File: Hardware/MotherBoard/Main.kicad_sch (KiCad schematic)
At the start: 12 parts, among them J11 DMA_PULLUP, U2 AT28C256, U3 WD65C22, U4 AS6C62256, U5 WD65C02

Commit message: Fix
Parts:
- added R7: 3K3, Resistor_THT:R_Axial_DIN0207_L6.3mm_D2.5mm_P10.16mm_Horizontal, symbol Device:R
- R2, R5: value 10K -> 3K3
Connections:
- net +5V: now also R7.1; no longer J11.2 (Pin_2)
- new net: J11.2 (Pin_2), R7.2
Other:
- title: Retro 6502 Mother Board -> Miniish
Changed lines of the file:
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@@
   (paper "A4")
   (title_block
-    (title "Retro 6502 Mother Board")
-    (rev "0.1")
+    (title "Miniish")
+    (rev "v1.2b")
     (company "Romuald Rousseau")
   )
@@
   (junction (at 135.382 94.996) (diameter 1.016) (color 0 0 0 0))
   (no_connect (at 51.816 120.65))
+  (no_connect (at 84.836 123.19))
+  (no_connect (at 51.816 135.89))
+  (no_connect (at 51.816 130.81))
   (no_connect (at 51.816 125.73))
-  (no_connect (at 51.816 135.89))
-  (no_connect (at 84.836 123.19))
-  (no_connect (at 51.816 130.81))
   (bus_entry (at 29.21 33.02) (size 2.54 -2.54)
     (stroke (width 0.1524) (type solid) (color 0 0 0 0))
@@
     (stroke (width 0) (type solid) (color 0 0 0 0))
   )
-  (wire (pts (xy 131.064 147.066) (xy 131.064 159.258))
+  (wire (pts (xy 131.064 147.066) (xy 131.064 148.59))
+    (stroke (width 0) (type solid) (color 0 0 0 0))
+  )
+  (wire (pts (xy 131.064 156.21) (xy 131.064 159.258))
     (stroke (width 0) (type solid) (color 0 0 0 0))
   )
@@
     (in_bom yes) (on_board yes)
     (property "Reference" "R5" (id 0) (at 45.466 118.11 90))
-    (property "Value" "10K" (id 1) (at 45.466 120.65 90))
+    (property "Value" "3K3" (id 1) (at 45.466 120.65 90))
     (property "Footprint" "Resistor_THT:R_Axial_DIN0207_L6.3mm_D2.5mm_P10.16mm_Horizontal" (id 2) (at 45.466 121.412 90)
       (effects (font (size 1.27 1.27)) hide)
@@
     (in_bom yes) (on_board yes)
     (property "Reference" "R2" (id 0) (at 97.282 120.65 90))
-    (property "Value" "10K" (id 1) (at 97.282 123.19 90))
+    (property "Value" "3K3" (id 1) (at 97.282 123.19 90))
     (property "Footprint" "Resistor_THT:R_Axial_DIN0207_L6.3mm_D2.5mm_P10.16mm_Horizontal" (id 2) (at 97.536 123.952 90)
       (effects (font (size 1.27 1.27)) hide)
@@
       (effects (font (size 1.27 1.27)) hide)
     )
+  )
+  (symbol (lib_id "Device:R") (at 131.064 152.4 0) (unit 1)
+    (in_bom yes) (on_board yes)
+    (property "Reference" "R7" (id 0) (at 125.984 152.654 90))
+    (property "Value" "3K3" (id 1) (at 128.524 152.654 90))
+    (property "Footprint" "Resistor_THT:R_Axial_DIN0207_L6.3mm_D2.5mm_P10.16mm_Horizontal" (id 2) (at 129.286 152.4 90)
+      (effects (font (size 1.27 1.27)) hide)
+    )
+    (property "Datasheet" "" (id 3) (at 131.064 152.4 0)
+      (effects (font (size 1.27 1.27)) hide)
+    )

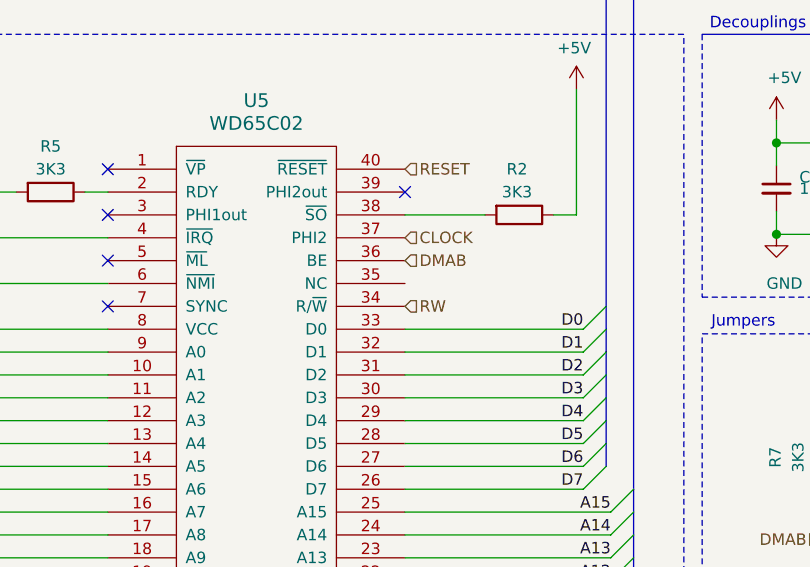
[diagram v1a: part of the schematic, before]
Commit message: Update to Kicad 6.0
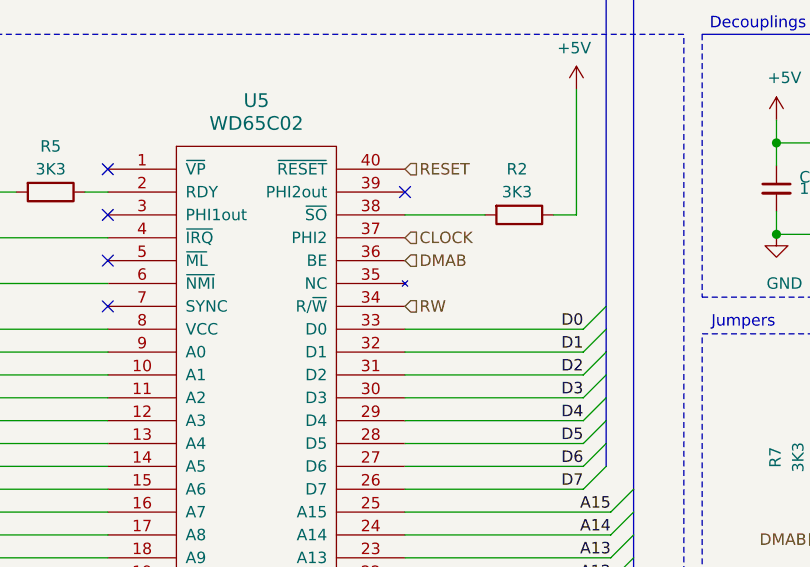
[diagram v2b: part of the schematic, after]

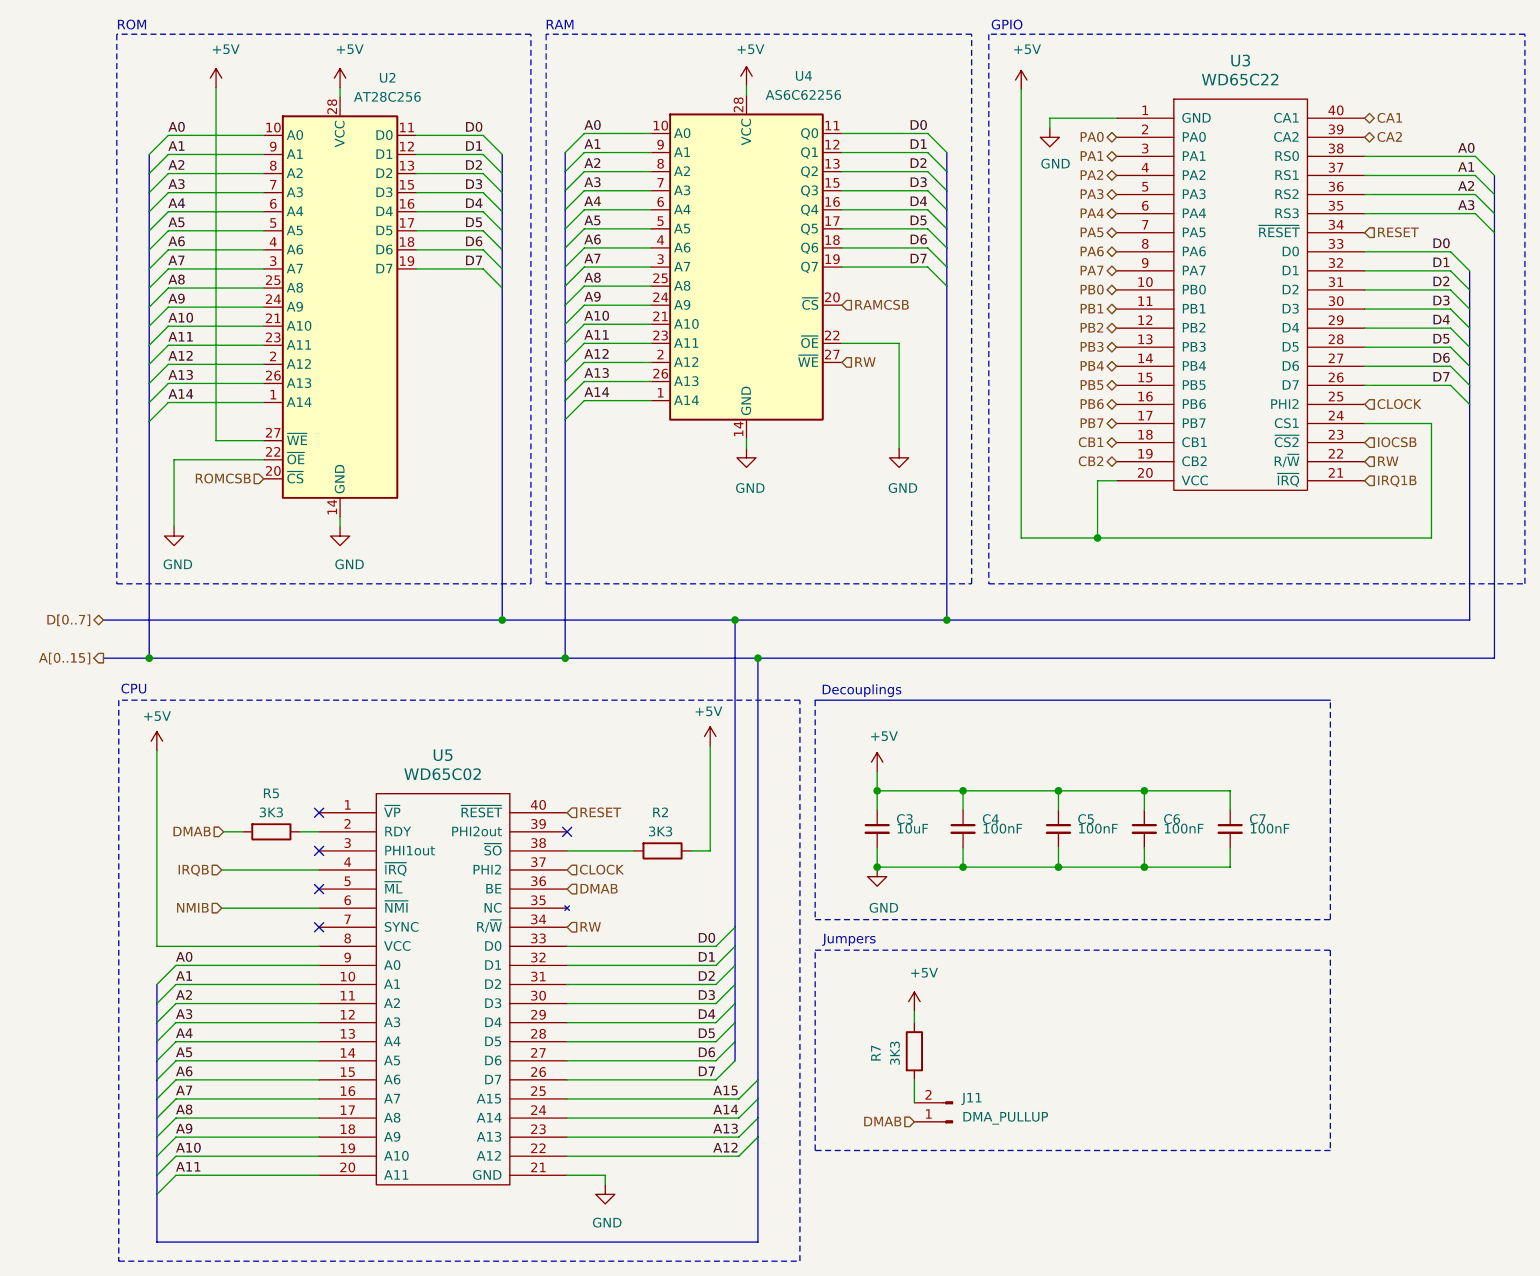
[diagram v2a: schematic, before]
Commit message: Fix Reset, WAI Signal, Add PROG jumper and reformat luc files
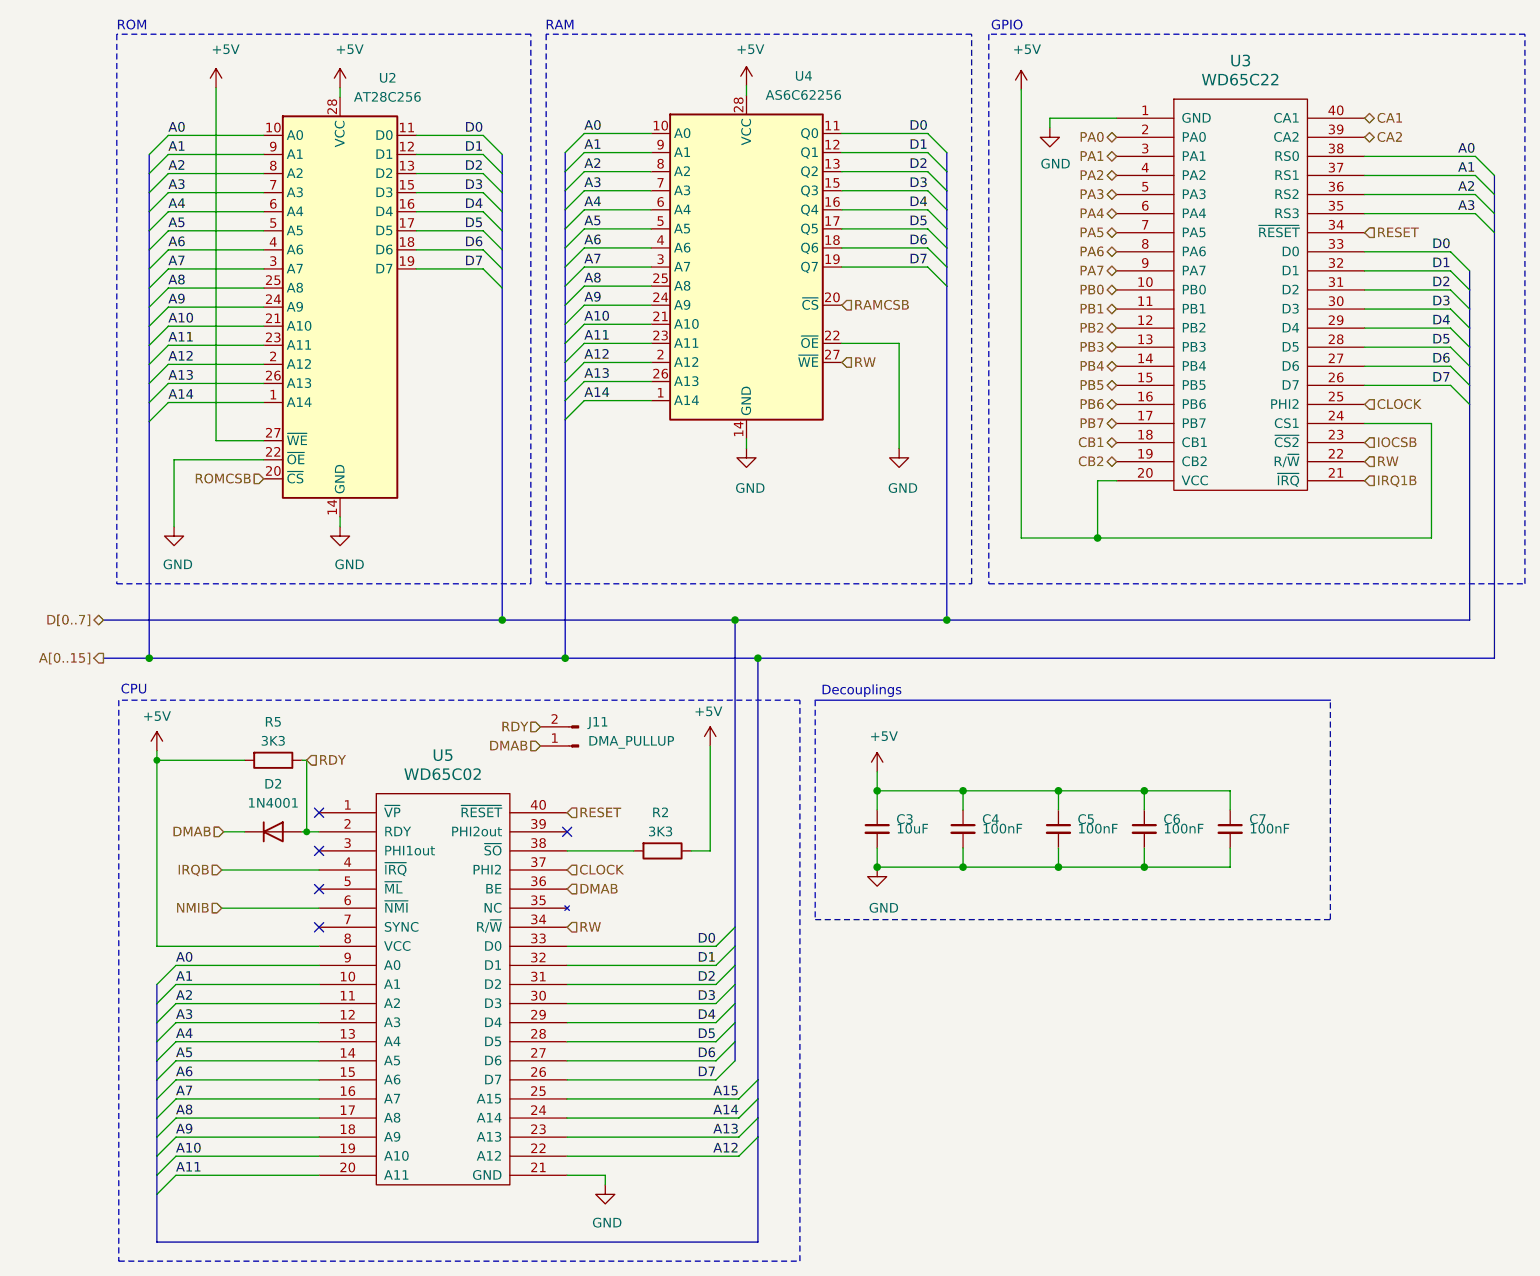
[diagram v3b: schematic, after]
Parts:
- removed R7: 3K3, Resistor_THT:R_Axial_DIN0207_L6.3mm_D2.5mm_P10.16mm_Horizontal, symbol Device:R
- added D2: 1N4001, Diode_THT:D_DO-41_SOD81_P10.16mm_Horizontal, symbol Diode:1N4001
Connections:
- net +5V: now also R5.2
- net DMAB: now also D2.1 (K); no longer R5.2
- net RDY: now reaches J11.2 (Pin_2)
- net RDY: now also R5.1, U5.2 (RDY), D2.2 (A)
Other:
- note removed: "Jumpers"
- moved on the sheet: J11, R5
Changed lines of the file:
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@@
     (company "Romuald Rousseau")
   )
+  (bus_alias "A" (members "A0" "A1" "A2" "A3" "A4" "A5" "A6" "A7"))
   (bus_alias "D" (members "D0" "D1" "D2"))
-  (bus_alias "A" (members "A0" "A1" "A2" "A3" "A4" "A5" "A6" "A7"))
   (junction (at 150.241 117.729) (diameter 1.016) (color 0 0 0 0)
   )
@@
   (junction (at 110.236 100.076) (diameter 1.016) (color 0 0 0 0)
   )
+  (junction (at 30.226 113.665) (diameter 0) (color 0 0 0 0)
+  )
   (junction (at 150.241 127.889) (diameter 1.016) (color 0 0 0 0)
   )
@@
   )
   (junction (at 84.582 100.076) (diameter 1.016) (color 0 0 0 0)
+  )
+  (junction (at 50.165 123.19) (diameter 0) (color 0 0 0 0)
   )
   (junction (at 137.541 127.889) (diameter 1.016) (color 0 0 0 0)
@@
     (stroke (width 0.1524) (type solid) (color 0 0 0 0))
   )
-  (polyline (pts (xy 186.436 138.938) (xy 186.436 165.608))
-    (stroke (width 0) (type dash) (color 0 0 0 0))
-  )
   (wire (pts (xy 173.101 127.889) (xy 173.101 125.349))
     (stroke (width 0) (type solid) (color 0 0 0 0))
@@
   (wire (pts (xy 31.75 55.88) (xy 44.45 55.88))
     (stroke (width 0) (type solid) (color 0 0 0 0))
-  )
-  (polyline (pts (xy 117.856 165.608) (xy 117.856 138.938))
-    (stroke (width 0) (type dash) (color 0 0 0 0))
   )
   (wire (pts (xy 31.75 53.34) (xy 44.45 53.34))
@@
     (stroke (width 0) (type solid) (color 0 0 0 0))
   )
+  (wire (pts (xy 30.226 113.665) (xy 30.226 138.43))
+    (stroke (width 0) (type solid) (color 0 0 0 0))
+  )
   (wire (pts (xy 121.412 35.306) (xy 132.842 35.306))
     (stroke (width 0) (type solid) (color 0 0 0 0))
   )
   (wire (pts (xy 191.008 40.894) (xy 205.74 40.894))
-    (stroke (width 0) (type solid) (color 0 0 0 0))
-  )
-  (wire (pts (xy 131.064 147.066) (xy 131.064 148.59))
     (stroke (width 0) (type solid) (color 0 0 0 0))
   )
@@
     (stroke (width 0) (type solid) (color 0 0 0 0))
   )
+  (wire (pts (xy 50.165 113.665) (xy 50.165 123.19))
+    (stroke (width 0) (type default) (color 0 0 0 0))
+  )
   (wire (pts (xy 191.008 56.134) (xy 202.438 56.134))
     (stroke (width 0) (type solid) (color 0 0 0 0))
@@
   (bus (pts (xy 208.28 35.814) (xy 208.28 38.354))
     (stroke (width 0) (type solid) (color 0 0 0 0))
+  )
+  (wire (pts (xy 50.165 123.19) (xy 51.816 123.19))
+    (stroke (width 0) (type default) (color 0 0 0 0))
   )
   (bus (pts (xy 29.21 100.076) (xy 84.582 100.076))
@@
     (stroke (width 0) (type solid) (color 0 0 0 0))
   )
-  (polyline (pts (xy 186.436 165.608) (xy 117.856 165.608))
-    (stroke (width 0) (type dash) (color 0 0 0 0))
-  )
   (wire (pts (xy 54.61 81.28) (xy 54.61 82.55))
     (stroke (width 0) (type solid) (color 0 0 0 0))
@@
     (stroke (width 0) (type solid) (color 0 0 0 0))
   )
+  (wire (pts (xy 49.53 113.665) (xy 50.165 113.665))
+    (stroke (width 0) (type default) (color 0 0 0 0))
+  )
   (wire (pts (xy 84.836 140.97) (xy 104.648 140.97))
     (stroke (width 0) (type solid) (color 0 0 0 0))
@@
     (stroke (width 0) (type solid) (color 0 0 0 0))
   )
-  (wire (pts (xy 30.226 138.43) (xy 30.226 112.395))
+  (wire (pts (xy 30.226 112.395) (xy 30.226 113.665))
     (stroke (width 0) (type solid) (color 0 0 0 0))
   )
@@
     (stroke (width 0) (type solid) (color 0 0 0 0))
   )
-  (wire (pts (xy 49.276 123.19) (xy 51.816 123.19))
-    (stroke (width 0) (type solid) (color 0 0 0 0))
-  )
   (bus (pts (xy 30.226 158.75) (xy 30.226 161.29))
     (stroke (width 0) (type solid) (color 0 0 0 0))
@@
     (stroke (width 0) (type solid) (color 0 0 0 0))
   )
+  (wire (pts (xy 49.53 123.19) (xy 50.165 123.19))
+    (stroke (width 0) (type default) (color 0 0 0 0))
+  )
   (wire (pts (xy 87.122 48.006) (xy 96.012 48.006))
     (stroke (width 0) (type solid) (color 0 0 0 0))
@@
     (stroke (width 0) (type solid) (color 0 0 0 0))
   )
-  (wire (pts (xy 39.116 123.19) (xy 41.656 123.19))
+  (wire (pts (xy 39.116 123.19) (xy 41.91 123.19))
     (stroke (width 0) (type solid) (color 0 0 0 0))
   )
@@
     (stroke (width 0) (type solid) (color 0 0 0 0))
   )
-  (polyline (pts (xy 117.856 138.938) (xy 186.436 138.938))
-    (stroke (width 0) (type dash) (color 0 0 0 0))
-  )
   (bus (pts (xy 107.188 148.59) (xy 107.188 151.13))
     (stroke (width 0) (type solid) (color 0 0 0 0))
@@
     (stroke (width 0) (type solid) (color 0 0 0 0))
   )
+  (wire (pts (xy 41.91 113.665) (xy 30.226 113.665))
+    (stroke (width 0) (type default) (color 0 0 0 0))
+  )
   (wire (pts (xy 191.008 68.834) (xy 199.898 68.834))
     (stroke (width 0) (type solid) (color 0 0 0 0))
   )
   (wire (pts (xy 145.288 24.384) (xy 145.288 84.074))
-    (stroke (width 0) (type solid) (color 0 0 0 0))
-  )
-  (wire (pts (xy 131.064 156.21) (xy 131.064 159.258))
     (stroke (width 0) (type solid) (color 0 0 0 0))
   )
@@
     (effects (font (size 1.27 1.27)) (justify right bottom))
   )
-  (text "Jumpers" (at 125.984 138.43 180)
-    (effects (font (size 1.27 1.27)) (justify right bottom))
-  )
   (text "RAM" (at 85.852 16.764 180)
     (effects (font (size 1.27 1.27)) (justify right bottom))
@@
     (effects (font (size 1.27 1.27)) (justify right))
   )
-  (hierarchical_label "DMAB" (shape input) (at 131.064 161.798 180)
+  (hierarchical_label "DMAB" (shape input) (at 81.28 111.76 180)
     (effects (font (size 1.27 1.27)) (justify right))
   )
@@
     (effects (font (size 1.27 1.27)) (justify right))
   )
+  (hierarchical_label "RDY" (shape input) (at 50.165 113.665 0)
+    (effects (font (size 1.27 1.27)) (justify left))
+  )
   (hierarchical_label "RW" (shape input) (at 84.836 135.89 0)
     (effects (font (size 1.27 1.27)) (justify left))
   )
+  (hierarchical_label "RDY" (shape input) (at 81.28 109.22 180)
+    (effects (font (size 1.27 1.27)) (justify right))
+  )
   (hierarchical_label "RAMCSB" (shape input) (at 121.412 53.086 0)
     (effects (font (size 1.27 1.27)) (justify left))
@@
     )
     (property "Datasheet" "" (id 3) (at 108.712 23.876 0)
-      (effects (font (size 1.27 1.27)) hide)
-    )
-    (pin "1")
-  )
-  (symbol (lib_id "power:+5V") (at 131.064 147.066 0) (unit 1)
-    (in_bom yes) (on_board yes)
-    (property "Reference" "#PWR08" (id 0) (at 131.064 150.876 0)
-      (effects (font (size 1.27 1.27)) hide)
-    )
-    (property "Value" "+5V" (id 1) (at 132.334 141.986 0))
-    (property "Footprint" "" (id 2) (at 131.064 147.066 0)
-      (effects (font (size 1.27 1.27)) hide)
-    )
-    (property "Datasheet" "" (id 3) (at 131.064 147.066 0)
       (effects (font (size 1.27 1.27)) hide)
     )
@@
     (pin "1")
   )
-  (symbol (lib_id "Device:R") (at 131.064 152.4 0) (unit 1)
-    (in_bom yes) (on_board yes)
-    (property "Reference" "R7" (id 0) (at 125.984 152.654 90))
-    (property "Value" "3K3" (id 1) (at 128.524 152.654 90))
-    (property "Footprint" "Resistor_THT:R_Axial_DIN0207_L6.3mm_D2.5mm_P10.16mm_Horizontal" (id 2) (at 129.286 152.4 90)
-      (effects (font (size 1.27 1.27)) hide)
-    )
-    (property "Datasheet" "" (id 3) (at 131.064 152.4 0)
-      (effects (font (size 1.27 1.27)) hide)
-    )
-    (pin "1")
-    (pin "2")
-  )
-  (symbol (lib_id "Device:R") (at 45.466 123.19 270) (unit 1)
-    (in_bom yes) (on_board yes)
-    (property "Reference" "R5" (id 0) (at 45.466 118.11 90))
-    (property "Value" "3K3" (id 1) (at 45.466 120.65 90))
-    (property "Footprint" "Resistor_THT:R_Axial_DIN0207_L6.3mm_D2.5mm_P10.16mm_Horizontal" (id 2) (at 45.466 121.412 90)
-      (effects (font (size 1.27 1.27)) hide)
-    )
-    (property "Datasheet" "" (id 3) (at 45.466 123.19 0)
+  (symbol (lib_id "Device:R") (at 45.72 113.665 270) (unit 1)
+    (in_bom yes) (on_board yes)
+    (property "Reference" "R5" (id 0) (at 45.72 108.585 90))
+    (property "Value" "3K3" (id 1) (at 45.72 111.125 90))
+    (property "Footprint" "Resistor_THT:R_Axial_DIN0207_L6.3mm_D2.5mm_P10.16mm_Horizontal" (id 2) (at 45.72 111.887 90)
+      (effects (font (size 1.27 1.27)) hide)
+    )
+    (property "Datasheet" "" (id 3) (at 45.72 113.665 0)
       (effects (font (size 1.27 1.27)) hide)
     )
@@
     (pin "9")
   )
-  (symbol (lib_id "Connector:Conn_01x02_Male") (at 136.144 161.798 180) (unit 1)
-    (in_bom yes) (on_board yes)
-    (property "Reference" "J11" (id 0) (at 137.414 158.623 0)
+  (symbol (lib_id "Diode:1N4001") (at 45.72 123.19 0) (unit 1)
+    (in_bom yes) (on_board yes) (fields_autoplaced)
+    (property "Reference" "D2" (id 0) (at 45.72 116.84 0))
+    (property "Value" "1N4001" (id 1) (at 45.72 119.38 0))
+    (property "Footprint" "Diode_THT:D_DO-41_SOD81_P10.16mm_Horizontal" (id 2) (at 45.72 127.635 0)
+      (effects (font (size 1.27 1.27)) hide)
+    )
+    (property "Datasheet" "http://www.vishay.com/docs/88503/1n4001.pdf" (id 3) (at 45.72 123.19 0)
+      (effects (font (size 1.27 1.27)) hide)
+    )
+    (pin "1")
+    (pin "2")
+  )
+  (symbol (lib_id "Connector:Conn_01x02_Male") (at 86.36 111.76 180) (unit 1)
+    (in_bom yes) (on_board yes)
+    (property "Reference" "J11" (id 0) (at 87.63 108.585 0)
       (effects (font (size 1.27 1.27)) (justify right))
     )
-    (property "Value" "DMA_PULLUP" (id 1) (at 137.414 161.163 0)
+    (property "Value" "DMA_PULLUP" (id 1) (at 87.63 111.125 0)
       (effects (font (size 1.27 1.27)) (justify right))
     )
-    (property "Footprint" "Connector_PinHeader_2.54mm:PinHeader_1x02_P2.54mm_Vertical" (id 2) (at 136.144 161.798 0)
-      (effects (font (size 1.27 1.27)) hide)
-    )
-    (property "Datasheet" "" (id 3) (at 136.144 161.798 0)
-      (effects (font (size 1.27 1.27)) hide)
-    )
+    (property "Footprint" "Connector_PinHeader_2.54mm:PinHeader_1x02_P2.54mm_Vertical" (id 2) (at 86.36 111.76 0)
+      (effects (font (size 1.27 1.27)) hide)
+    )
+    (property "Datasheet" "" (id 3) (at 86.36 111.76 0)
+      (effects (font (size 1.27 1.27)) hide)
+    )
